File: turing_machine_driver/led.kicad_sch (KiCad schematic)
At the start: 60 parts, among them U10 74LS245, U11 SST39SF020, U12 74LS245, U13 74LS245, U14 74LS245, U15 D5631LA, U16 D5631LR, U17 74LS245, U3 74LS04, U4 74LS139, U5 74LS74, U9 74LS245

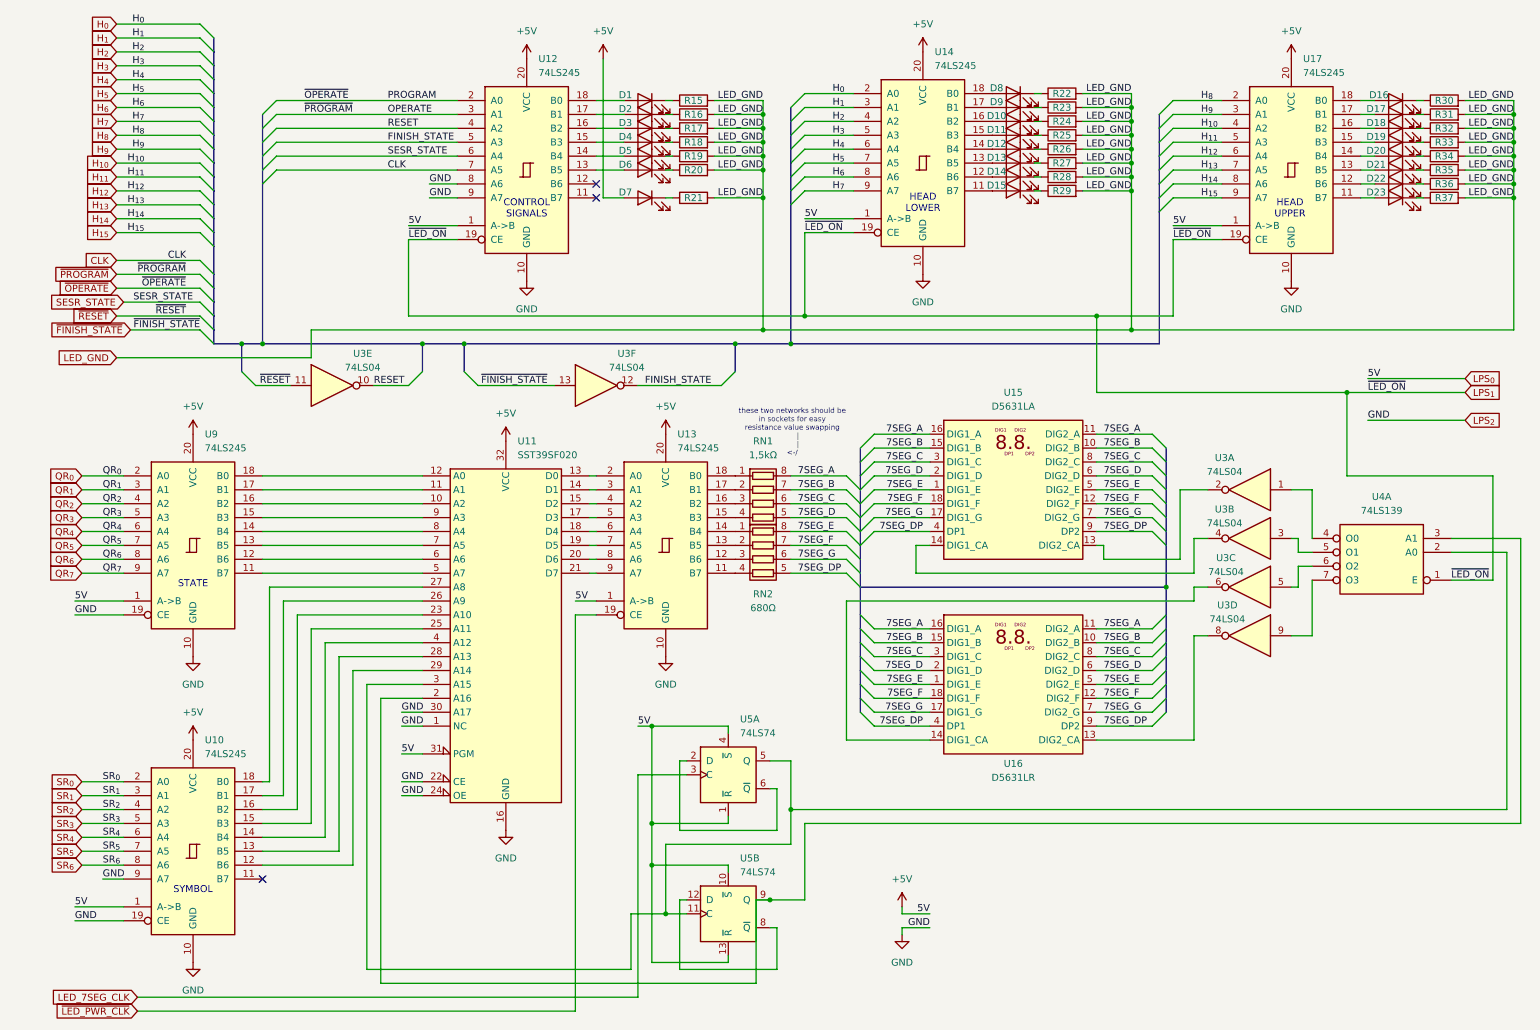
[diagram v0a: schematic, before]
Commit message: added control panel and moved LEDs to it
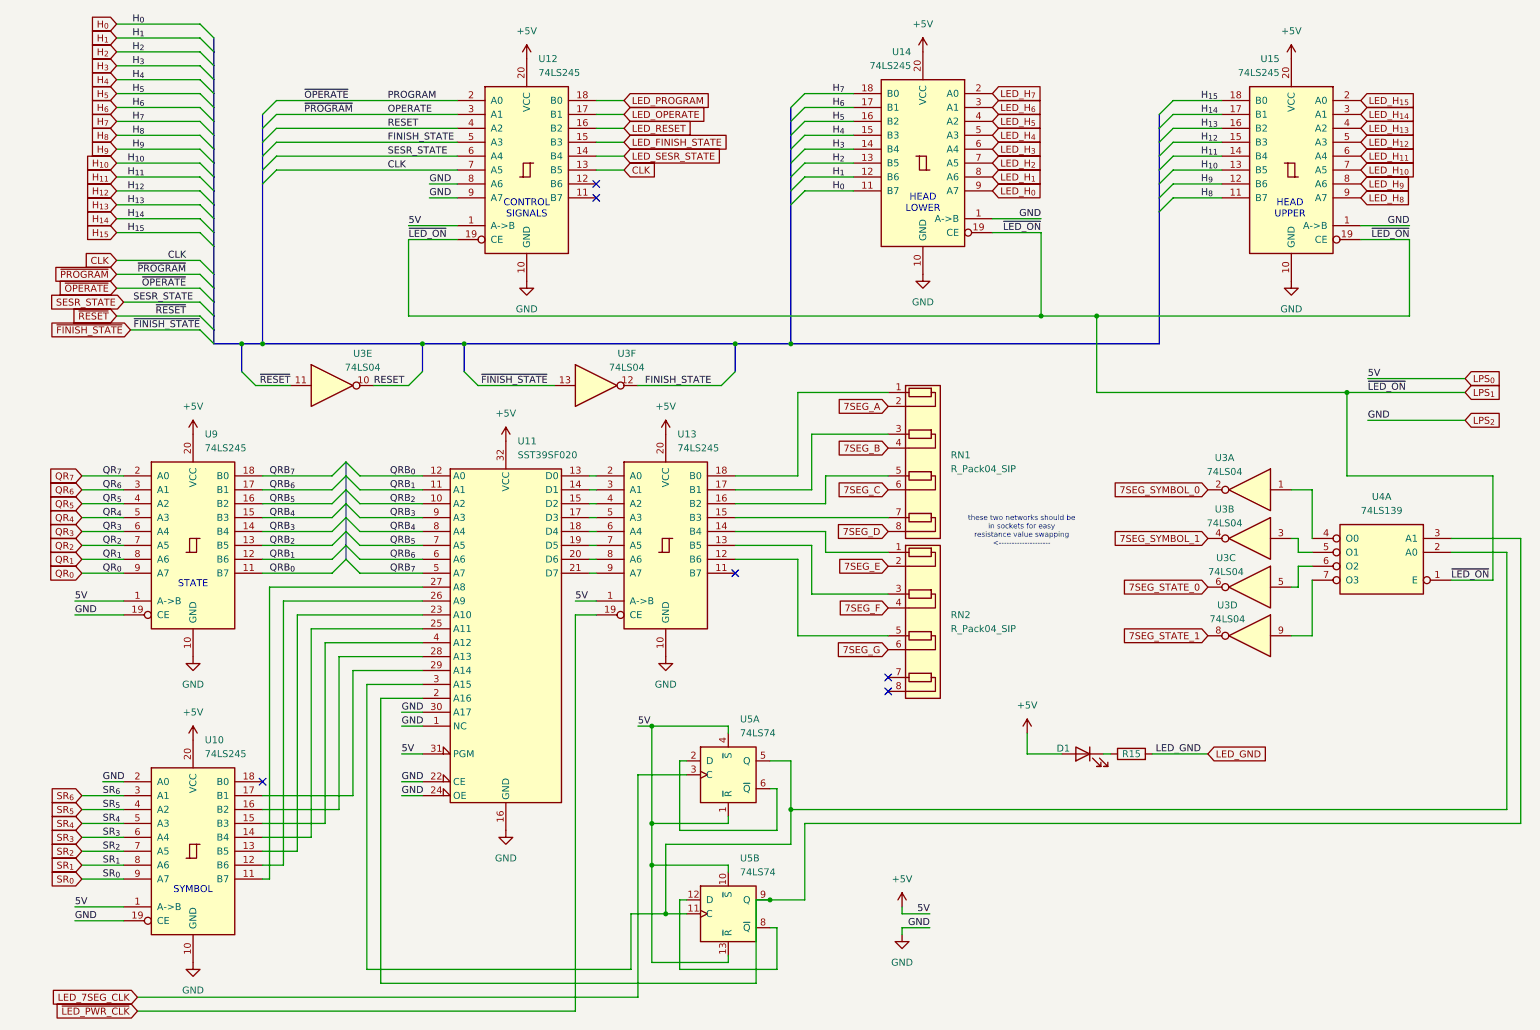
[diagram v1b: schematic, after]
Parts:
- removed D1: LED_OPERATE_R, LED_THT:LED_D5.0mm, symbol Device:LED
- removed D10: LED_HEADER2, LED_THT:LED_D5.0mm, symbol Device:LED
- removed D11: LED_HEADER3, LED_THT:LED_D5.0mm, symbol Device:LED
- removed D12: LED_HEADER4, LED_THT:LED_D5.0mm, symbol Device:LED
- removed D13: LED_HEADER5, LED_THT:LED_D5.0mm, symbol Device:LED
- removed D14: LED_HEADER6, LED_THT:LED_D5.0mm, symbol Device:LED
- removed D15: LED_HEADER7, LED_THT:LED_D5.0mm, symbol Device:LED
- removed D16: LED_HEADER8, LED_THT:LED_D5.0mm, symbol Device:LED
- removed D17: LED_HEADER9, LED_THT:LED_D5.0mm, symbol Device:LED
- removed D18: LED_HEADER10, LED_THT:LED_D5.0mm, symbol Device:LED
- removed D19: LED_HEADER11, LED_THT:LED_D5.0mm, symbol Device:LED
- removed D2: LED_PROGRAM_R, LED_THT:LED_D5.0mm, symbol Device:LED
- removed D20: LED_HEADER12, LED_THT:LED_D5.0mm, symbol Device:LED
- removed D21: LED_HEADER13, LED_THT:LED_D5.0mm, symbol Device:LED
- removed D22: LED_HEADER14, LED_THT:LED_D5.0mm, symbol Device:LED
- removed D23: LED_HEADER15, LED_THT:LED_D5.0mm, symbol Device:LED
- removed D3: LED_RESET_Y, LED_THT:LED_D5.0mm, symbol Device:LED
- removed D4: LED_FINISH_STATE_Y, LED_THT:LED_D5.0mm, symbol Device:LED
- removed D5: LED_SESR_STATE_G, LED_THT:LED_D5.0mm, symbol Device:LED
- removed D6: LED_CLK_G, LED_THT:LED_D5.0mm, symbol Device:LED
- removed D8: LED_HEADER0, LED_THT:LED_D5.0mm, symbol Device:LED
- removed D9: LED_HEADER1, LED_THT:LED_D5.0mm, symbol Device:LED
- removed R15, R16, R17, R18, R19, R20, R22, R23, R24, R25, R26, R27, R28, R29, R30, R31, R32, R33, R34, R35, R36, R37: 330Ω, Resistor_THT:R_Axial_DIN0207_L6.3mm_D2.5mm_P10.16mm_Horizontal, symbol Device:R
- removed RN1: 1,5kΩ, Connector_PinSocket_2.54mm:PinSocket_1x08_P2.54mm_Vertical, symbol Device:R_Pack04
- removed RN2: 680Ω, Connector_PinSocket_2.54mm:PinSocket_1x08_P2.54mm_Vertical, symbol Device:R_Pack04
- removed U15: D5631LA, Display_7Segment:DA56-11CGKWA, symbol Display_Character:DA56-11CGKWA
- removed U16: D5631LR, Display_7Segment:DA56-11CGKWA, symbol Display_Character:DA56-11CGKWA
- added RN1, RN2: R_Pack04_SIP, Resistor_THT:R_Array_SIP8, symbol Device:R_Pack04_SIP
- renumbered D7 to D1, R21 to R15, U17 to U15
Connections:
- net +5V: no longer U14.1 (A->B), U15.1 (A->B)
- net 7SEG_A: now also RN1.2 (R1.2)
- net 7SEG_B: now also RN1.4 (R2.2)
- net 7SEG_C: now also RN1.6 (R3.2)
- net 7SEG_D: now also RN1.8 (R4.2)
- net 7SEG_E: now also RN2.2 (R1.2)
- net 7SEG_F: now also RN2.4 (R2.2)
- net 7SEG_G: now also RN2.6 (R3.2)
- net CLK: now also U12.13 (B5)
- net GND: now also U10.2 (A0), U14.1 (A->B), U15.1 (A->B); no longer U10.9 (A7)
- net H_{0}: now also U14.11 (B7); no longer U14.2 (A0)
- net H_{10}: now also U15.13 (B5); no longer U15.4 (A2)
- net H_{11}: now also U15.14 (B4); no longer U15.5 (A3)
- net H_{12}: now also U15.15 (B3); no longer U15.6 (A4)
- net H_{13}: now also U15.16 (B2); no longer U15.7 (A5)
- net H_{14}: now also U15.17 (B1); no longer U15.8 (A6)
- net H_{15}: now also U15.18 (B0); no longer U15.9 (A7)
- net H_{1}: now also U14.12 (B6); no longer U14.3 (A1)
- net H_{2}: now also U14.13 (B5); no longer U14.4 (A2)
- net H_{3}: now also U14.14 (B4); no longer U14.5 (A3)
- net H_{4}: now also U14.15 (B3); no longer U14.6 (A4)
- net H_{5}: now also U14.16 (B2); no longer U14.7 (A5)
- net H_{6}: now also U14.17 (B1); no longer U14.8 (A6)
- net H_{7}: now also U14.18 (B0); no longer U14.9 (A7)
- net H_{8}: now also U15.11 (B7); no longer U15.2 (A0)
- net H_{9}: now also U15.12 (B6); no longer U15.3 (A1)
- net QR_{0}: now also U9.9 (A7); no longer U9.2 (A0)
- net QR_{1}: now also U9.8 (A6); no longer U9.3 (A1)
- net QR_{2}: now also U9.7 (A5); no longer U9.4 (A2)
- net QR_{3}: now also U9.6 (A4); no longer U9.5 (A3)
- net QR_{4}: now also U9.5 (A3); no longer U9.6 (A4)
- net QR_{5}: now also U9.4 (A2); no longer U9.7 (A5)
- net QR_{6}: now also U9.3 (A1); no longer U9.8 (A6)
- net QR_{7}: now also U9.2 (A0); no longer U9.9 (A7)
- net SR_{0}: now also U10.9 (A7); no longer U10.2 (A0)
- net SR_{1}: now also U10.8 (A6); no longer U10.3 (A1)
- net SR_{2}: now also U10.7 (A5); no longer U10.4 (A2)
- net SR_{3}: now also U10.6 (A4); no longer U10.5 (A3)
- net SR_{4}: now also U10.5 (A3); no longer U10.6 (A4)
- net SR_{5}: now also U10.4 (A2); no longer U10.7 (A5)
- net SR_{6}: now also U10.3 (A1); no longer U10.8 (A6)
- net LED_SESR_STATE: now reaches U12.14 (B4)
- net 7SEG_STATE_1: now reaches U3.8
- net 7SEG_STATE_0: now reaches U3.6
- net 7SEG_SYMBOL_1: now reaches U3.4
- net 7SEG_SYMBOL_0: now reaches U3.2
- net at U13.12 (B6): now also RN2.5 (R3.1)
- net at U13.13 (B5): now also RN2.3 (R2.1)
- net at U13.14 (B4): now also RN2.1 (R1.1)
- net at U13.15 (B3): now also RN1.7 (R4.1)
- net at U13.16 (B2): now also RN1.5 (R3.1)
- net at U13.17 (B1): now also RN1.3 (R2.1)
- net at U13.18 (B0): now also RN1.1 (R1.1)
- net at U10.11 (B7): now also U11.27 (A8)
- net at U10.12 (B6): now also U11.26 (A9); no longer U11.29 (A14)
- net at U10.13 (B5): now also U11.23 (A10); no longer U11.28 (A13)
- net at U10.14 (B4): now also U11.25 (A11); no longer U11.4 (A12)
- net at U10.15 (B3): now also U11.4 (A12); no longer U11.25 (A11)
- net at U10.16 (B2): now also U11.28 (A13); no longer U11.23 (A10)
- net at U10.17 (B1): now also U11.29 (A14); no longer U11.26 (A9)
- net at U10.18 (B0): no longer U11.27 (A8)
- net LED_FINISH_STATE: now reaches U12.15 (B3)
- net LED_RESET: now reaches U12.16 (B2)
- net LED_OPERATE: now reaches U12.17 (B1)
- net LED_PROGRAM: now reaches U12.18 (B0)
- net QRB_{2}: now reaches U11.10 (A2)
- net QRB_{2}: now also U9.13 (B5); no longer U9.16 (B2)
- net QRB_{1}: now reaches U11.11 (A1)
- net QRB_{1}: now also U9.12 (B6); no longer U9.17 (B1)
- net QRB_{0}: now reaches U11.12 (A0)
- net QRB_{0}: now also U9.11 (B7); no longer U9.18 (B0)
- net QRB_{7}: now reaches U11.5 (A7)
- net QRB_{7}: now also U9.18 (B0); no longer U9.11 (B7)
- net QRB_{6}: now reaches U11.6 (A6)
- net QRB_{6}: now also U9.17 (B1); no longer U9.12 (B6)
- net QRB_{5}: now reaches U11.7 (A5)
- net QRB_{5}: now also U9.16 (B2); no longer U9.13 (B5)
- net QRB_{3}: now reaches U9.14 (B4)
- net QRB_{3}: now also U11.9 (A3); no longer U11.8 (A4)
- net QRB_{4}: now reaches U9.15 (B3)
- net QRB_{4}: now also U11.8 (A4); no longer U11.9 (A3)
- new net LED_H_{0}: U14.9 (A7)
- new net LED_H_{10}: U15.7 (A5)
- new net LED_H_{11}: U15.6 (A4)
- new net LED_H_{12}: U15.5 (A3)
- new net LED_H_{13}: U15.4 (A2)
- new net LED_H_{14}: U15.3 (A1)
- new net LED_H_{15}: U15.2 (A0)
- new net LED_H_{1}: U14.8 (A6)
- new net LED_H_{2}: U14.7 (A5)
- new net LED_H_{3}: U14.6 (A4)
- new net LED_H_{4}: U14.5 (A3)
- new net LED_H_{5}: U14.4 (A2)
- new net LED_H_{6}: U14.3 (A1)
- new net LED_H_{7}: U14.2 (A0)
- new net LED_H_{8}: U15.9 (A7)
- new net LED_H_{9}: U15.8 (A6)
- no-connect marks 3 -> 6
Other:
- note added: "these two networks should be in sockets for easy resistance value swapping <--------------------"
- note removed: "these two networks should be in sockets for easy resistance value swapping | | <-/"
- moved on the sheet: D1, R15

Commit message: added some wiring and fixed few schematic bugs
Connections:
- net LED_GND is gone; now on net GND: R15.2
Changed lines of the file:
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@@
+	)
+	(label "GND"
+		(at 224.79 148.59 180)
+		(effects
+			(font
+				(size 1.27 1.27)
+			)
+			(justify right bottom)
+		)
 	)
 	(label "GND"
@@
 		)
 	)
-	(label "LED_GND"
-		(at 223.52 148.59 180)
-		(effects
-			(font
-				(size 1.27 1.27)
-			)
-			(justify right bottom)
-		)
-	)
 	(label "5V"
 		(at 78.74 52.07 0)
@@
 			(effects
 				(font
-					(size 1.27 1.27)
-				)
-				(justify left)
-				(hide yes)
-			)
-		)
-	)
-	(global_label "LED_GND"
-		(shape input)
-		(at 224.79 148.59 0)
-		(fields_autoplaced yes)
-		(effects
-			(font
-				(size 1.27 1.27)
-			)
-			(justify left)
-		)
-		(property "Intersheetrefs" "${INTERSHEET_REFS}"
-			(at 236.0604 148.59 0)
-			(effects
-				(font
